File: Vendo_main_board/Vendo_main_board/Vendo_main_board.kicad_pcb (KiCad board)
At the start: 2 copper layers, 49 x 99 mm, 121 parts, among them J1 STLINK, J10 Screw_Terminal_01x04, J11 Screw_Terminal_01x04, J12 Screw_Terminal_01x02, J13 Screw_Terminal_01x02, J14 197084013, J15 197084013, J16 197084013, J17 197084013, J18 197084013, J19 FTDI, J2 Conn_01x02_Pin, J21 Conn_01x04_Pin, J23 BOOT, J5 Screw_Terminal_01x03, J6 Conn_01x06_Pin, J7 Conn_01x06_Pin, J8 Screw_Terminal_01x04, J9 Screw_Terminal_01x04, K1 SRD-05VDC-SL-C, Q3 S8050, Q4 Q_NMOS_Depletion_GSD, SW1 SW_Push, SW2 SW_DIP_x08, U1 AP64350SP-13, U10 74HC165, U11 PC817, U12 PC817, U2 AMS1117-3.3, U3 B0505S-2WR3, U4 TPL5010, U9 STM32F103C8T6, Y1 8MHz, Y2 32.768kHz

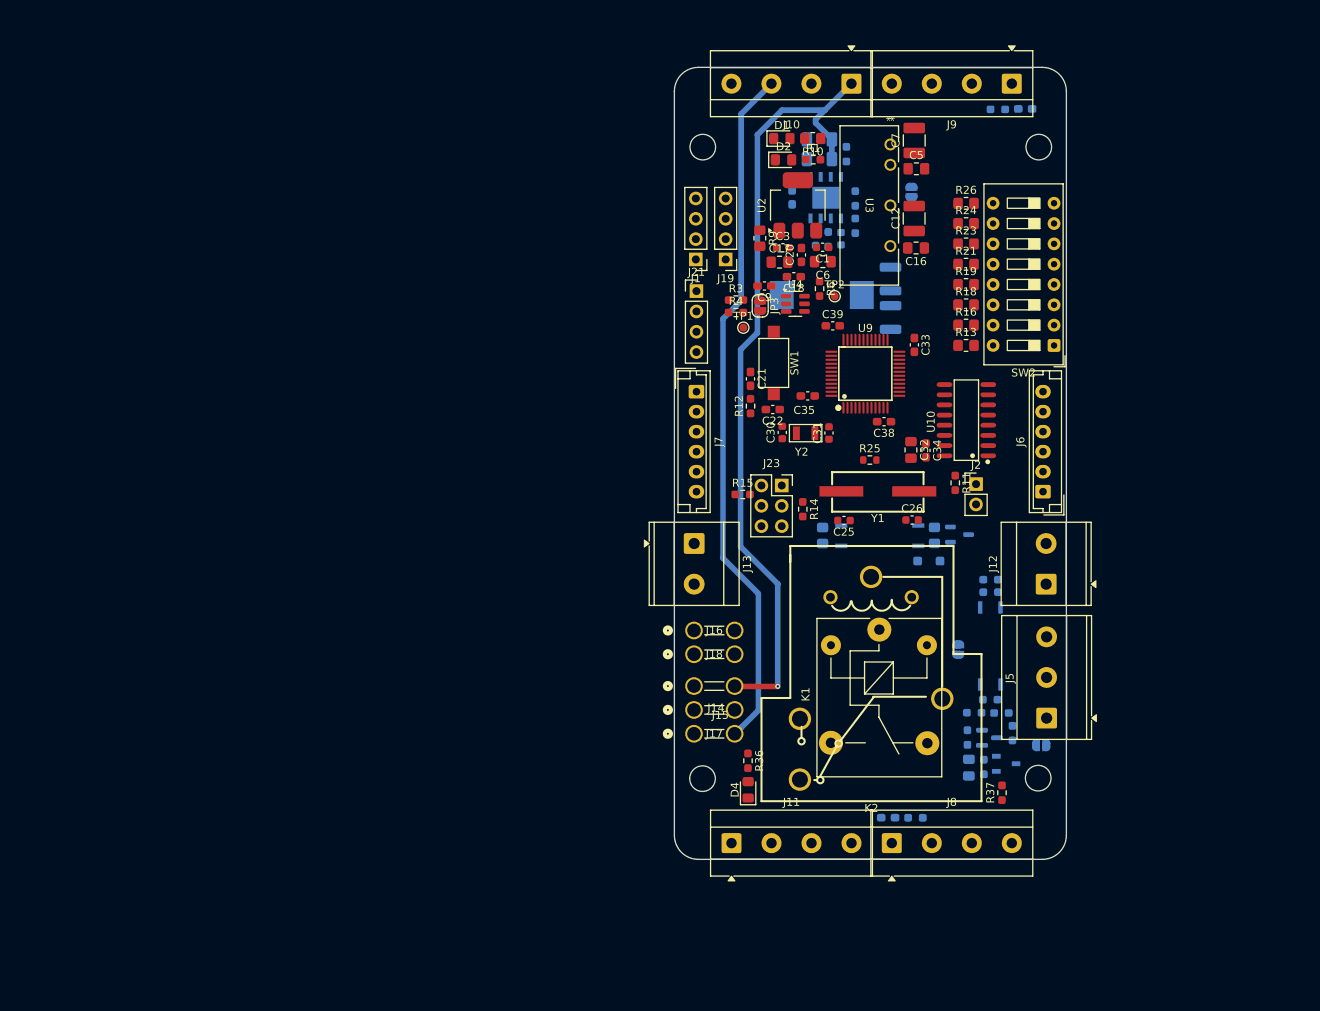
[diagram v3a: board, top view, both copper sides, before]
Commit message: -scheme update by charles
1. Used standard input and output nodes
2. Fixed GND connection of BOOT0 and BOOT1 (initially connected to Analog GND)
3. Removed redundant 100K pull up WDT RST Pin
4. Removed Nets on unconnected STM Pins
5. Fixed GND of Oscillator
6. Added 5V and 12V option to LED, removed LED as direct LED Drive
7. Renamed ESP INT to I2C INT
8. Changed 12V to 12VA, removed nets, used power rail symbol instead
9. Simplified 12V Logic
10. removed WDT, STM has internal WDT
11. Added DPDT Config to Relay Logic
12. Added Pullup I2C Line
13. Fixed 5V logic with 3.3V V Logic on 7Seg Driver
14. Added Auxiliary Pins
15.Added Debug LEDs,
Updated Footprints
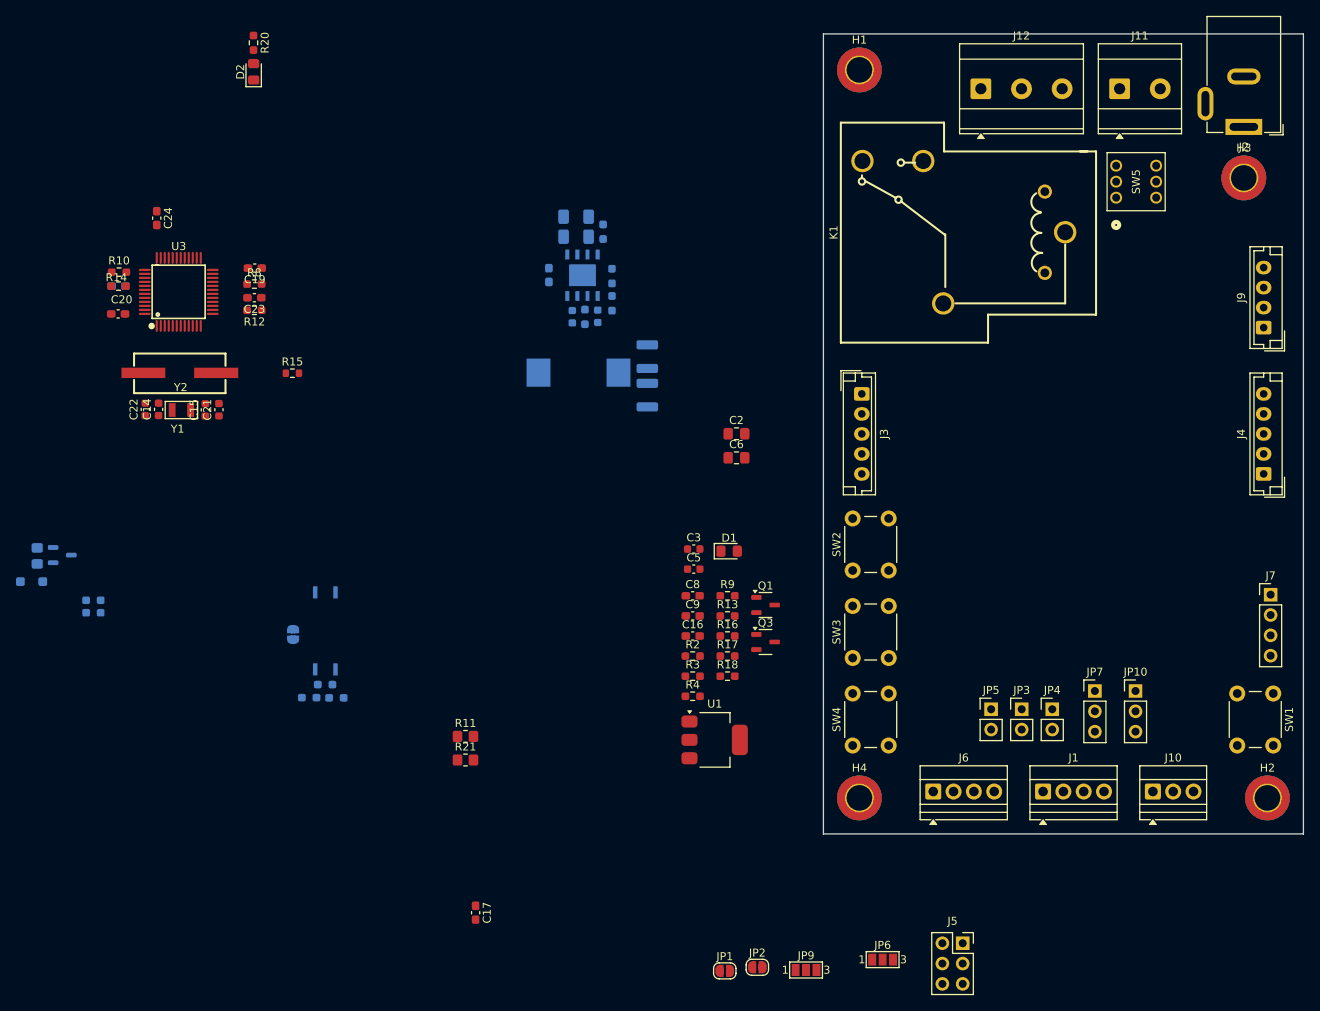
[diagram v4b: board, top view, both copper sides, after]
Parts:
- removed the C1 at (198.0, 54.3)
- removed the C12 at (209.4, 50.7)
- removed the C17 at (192.6, 56.1)
- removed the C18 at (194.4, 58.0)
- removed the C20 at (195.3, 55.2)
- removed the C22 at (191.8, 74.5)
- removed C32, C40: 10uF, Capacitor_SMD:C_0805_2012Metric_Pad1.18x1.45mm_HandSolder
- removed C34, C36: 100nF, Capacitor_SMD:C_0603_1608Metric_Pad1.08x0.95mm_HandSolder
- removed the C7 at (209.4, 40.9)
- removed the D2 at (193.1, 43.3)
- removed J13: Screw_Terminal_01x02, TerminalBlock_MetzConnect:TerminalBlock_MetzConnect_Type073_RT02602HBLU_1x02_P5.08mm_Horizontal
- removed J14, J15, J16, J17, J18: 197084013, InnovKits:Spade Conn4.8mm
- removed J19: FTDI, Connector_PinHeader_2.54mm:PinHeader_1x04_P2.54mm_Vertical
- removed J21: Conn_01x04_Pin, Connector_PinHeader_2.54mm:PinHeader_1x04_P2.54mm_Vertical
- removed the J5 at (226.0, 113.1)
- removed J8: Screw_Terminal_01x04, TerminalBlock_MetzConnect:TerminalBlock_MetzConnect_Type055_RT01504HDWU_1x04_P5.00mm_Horizontal
- removed the K1 at (205.1, 102.1)
- removed Q5: ~, footprints:SOT-23-3_L2.9-W1.6-P1.90-LS2.8-BR
- removed the R1 at (196.8, 43.3)
- removed the R10 at (196.8, 40.7)
- removed the R15 at (188.0, 85.2)
- removed the R19 at (215.9, 58.9)
- removed the R23 at (215.9, 53.9)
- removed the R24 at (215.9, 51.3)
- removed the R26 at (215.9, 48.8)
- removed R31: 10K, Resistor_SMD:R_0805_2012Metric_Pad1.20x1.40mm_HandSolder
- removed R34: 4.7k, Resistor_SMD:R_0603_1608Metric_Pad0.98x0.95mm_HandSolder
- removed R37: 1k, Resistor_SMD:R_0603_1608Metric_Pad0.98x0.95mm_HandSolder
- removed R39: 100k, Resistor_SMD:R_0603_1608Metric_Pad0.98x0.95mm_HandSolder
- removed R40: 100, Resistor_SMD:R_0603_1608Metric_Pad0.98x0.95mm_HandSolder
- removed the R6 at (197.6, 59.5)
- removed TP1, TP2: TestPoint, TestPoint:TestPoint_Pad_D1.0mm
- removed U10: 74HC165, InnovKits:SOIC-16_L9.9-W3.9-P1.27-LS6.0-BL
- removed U11: PC817, InnovKits:APC-817xx-SL_AMB
- removed the U2 at (194.9, 49.0)
- removed the U3 at (206.5, 41.4)
- removed the U4 at (194.6, 61.3)
- added C2: 1uF, Capacitor_SMD:C_0805_2012Metric_Pad1.18x1.45mm_HandSolder, F.Cu at (187.2, 77.6)
- added C8: 100nF, Capacitor_SMD:C_0603_1608Metric_Pad1.08x0.95mm_HandSolder, F.Cu at (181.8, 97.8)
- added J3: Conn_01x05_Pin, Connector_JST:JST_EH_B5B-EH-A_1x05_P2.50mm_Vertical, F.Cu at (202.9, 72.6)
- added J4: Conn_01x05_Pin, Connector_JST:JST_EH_B5B-EH-A_1x05_P2.50mm_Vertical, F.Cu at (253.1, 82.6)
- added JP10: Jumper_3_Open, Connector_PinHeader_2.54mm:PinHeader_1x03_P2.54mm_Vertical, F.Cu at (237.1, 109.7)
- added JP2: SolderJumper_2_Open, Jumper:SolderJumper-2_P1.3mm_Open_RoundedPad1.0x1.5mm, F.Cu at (189.8, 144.3)
- added JP4: SolderJumper_2_Open, Connector_PinHeader_2.54mm:PinHeader_1x02_P2.54mm_Vertical, F.Cu at (226.7, 112.0)
- added JP6: SolderJumper_3_Open, Jumper:SolderJumper-3_P1.3mm_Open_Pad1.0x1.5mm_NumberLabels, F.Cu at (205.5, 143.3)
- added JP7: Jumper_3_Open, Connector_PinHeader_2.54mm:PinHeader_1x03_P2.54mm_Vertical, F.Cu at (232.0, 109.7)
- added JP9: SolderJumper_3_Open, Jumper:SolderJumper-3_P1.3mm_Open_Pad1.0x1.5mm_NumberLabels, F.Cu at (195.9, 144.6)
- added Q1: Q_NMOS_Depletion_GSD, Package_TO_SOT_SMD:SOT-23-3, F.Cu at (190.9, 99.0)
- added R17: 100K, Resistor_SMD:R_0603_1608Metric_Pad0.98x0.95mm_HandSolder, F.Cu at (186.1, 105.4)
- added R2: 4.7K, Resistor_SMD:R_0603_1608Metric_Pad0.98x0.95mm_HandSolder, F.Cu at (181.8, 105.4)
- added SW3: SW_Push, Button_Switch_THT:SW_PUSH_6mm_H5mm, F.Cu at (201.8, 105.6)
- added SW4: SW_Push, Button_Switch_THT:SW_PUSH_6mm_H5mm, F.Cu at (201.8, 116.5)
- added SW5: SW_Slide_DPDT, InnovKits:DPDT_PUSH, F.Cu at (234.7, 48.1)
- added U1: AMS1117-3.3, Package_TO_SOT_SMD:SOT-223-3_TabPin2, F.Cu at (184.5, 115.8)
- C16: value 10uF -> 100nF; footprint Capacitor_SMD:C_0805_2012Metric_Pad1.18x1.45mm_HandSolder -> Capacitor_SMD:C_0603_1608Metric_Pad1.08x0.95mm_HandSolder
- C17: renamed from C21; value 100nF -> 1uF
- C5: value 10uF -> 22uF; footprint Capacitor_SMD:C_0805_2012Metric_Pad1.18x1.45mm_HandSolder -> Capacitor_SMD:C_0603_1608Metric
- C9: value 100nF -> 10uF
- H1, H2, H3, H4: footprint MountingHole:MountingHole_3.2mm_M3 -> MountingHole:MountingHole_3.2mm_M3_DIN965_Pad_TopBottom
- J1: value STLINK -> Screw_Terminal_01x04; footprint Connector_PinHeader_2.54mm:PinHeader_1x04_P2.54mm_Vertical -> TerminalBlock:TerminalBlock_Xinya_XY308-2.54-4P_1x04_P2.54mm_Horizontal
- J10: value Screw_Terminal_01x04 -> Screw_Terminal_01x03; footprint TerminalBlock_MetzConnect:TerminalBlock_MetzConnect_Type055_RT01504HDWU_1x04_P5.00mm_Horizontal -> TerminalBlock:TerminalBlock_Xinya_XY308-2.54-3P_1x03_P2.54mm_Horizontal
- J11: value Screw_Terminal_01x04 -> Screw_Terminal_01x02; footprint TerminalBlock_MetzConnect:TerminalBlock_MetzConnect_Type055_RT01504HDWU_1x04_P5.00mm_Horizontal -> TerminalBlock_MetzConnect:TerminalBlock_MetzConnect_Type073_RT02602HBLU_1x02_P5.08mm_Horizontal
- J12: value Screw_Terminal_01x02 -> Screw_Terminal_01x03; footprint TerminalBlock_MetzConnect:TerminalBlock_MetzConnect_Type073_RT02602HBLU_1x02_P5.08mm_Horizontal -> TerminalBlock_MetzConnect:TerminalBlock_MetzConnect_Type073_RT02603HBLU_1x03_P5.08mm_Horizontal
- J2: value Conn_01x02_Pin -> Barrel_Jack_MountingPin; footprint Connector_PinHeader_2.54mm:PinHeader_1x02_P2.54mm_Vertical -> Connector_BarrelJack:BarrelJack_GCT_DCJ200-10-A_Horizontal
- J6: value Conn_01x06_Pin -> Screw_Terminal_01x04; footprint Connector_JST:JST_EH_B6B-EH-A_1x06_P2.50mm_Vertical -> TerminalBlock:TerminalBlock_Xinya_XY308-2.54-4P_1x04_P2.54mm_Horizontal
- J7: value Conn_01x06_Pin -> FTDI; footprint Connector_JST:JST_EH_B6B-EH-A_1x06_P2.50mm_Vertical -> Connector_PinHeader_2.54mm:PinHeader_1x04_P2.54mm_Vertical
- J9: value Screw_Terminal_01x04 -> Conn_01x04_Pin; footprint TerminalBlock_MetzConnect:TerminalBlock_MetzConnect_Type055_RT01504HDWU_1x04_P5.00mm_Horizontal -> Connector_JST:JST_EH_B4B-EH-A_1x04_P2.50mm_Vertical
- JP1: moved to F.Cu
- JP3: footprint Jumper:SolderJumper-2_P1.3mm_Open_RoundedPad1.0x1.5mm -> Connector_PinHeader_2.54mm:PinHeader_1x02_P2.54mm_Vertical
- JP5: footprint Jumper:SolderJumper-2_P1.3mm_Open_RoundedPad1.0x1.5mm -> Connector_PinHeader_2.54mm:PinHeader_1x02_P2.54mm_Vertical; moved to F.Cu
- Q3: value S8050 -> Q_NMOS_Depletion_GSD; footprint Package_TO_SOT_SMD:SOT-23 -> Package_TO_SOT_SMD:SOT-23-3; moved to F.Cu
- R10: renamed from R29; value 1k -> 1K; moved to F.Cu
- R11: value 1k -> 10K; footprint Resistor_SMD:R_0603_1608Metric_Pad0.98x0.95mm_HandSolder -> Resistor_SMD:R_0805_2012Metric_Pad1.20x1.40mm_HandSolder
- R12: value 1k -> 10K
- R13, R16, R18: footprint Resistor_SMD:R_0805_2012Metric_Pad1.20x1.40mm_HandSolder -> Resistor_SMD:R_0603_1608Metric_Pad0.98x0.95mm_HandSolder
- R14: renamed from R30; moved to F.Cu
- R20: renamed from R36; value 1k -> 1K
- R22: renamed from R32; value 1k -> 1K
- R24: renamed from R35; value 1k -> 1K
- R25: renamed from R41; value 1k -> 1K
- R3: value 10K -> 4.7K
- R4: value 40.2K -> 1K
- R9: value 3.3K -> 100k; footprint Resistor_SMD:R_0805_2012Metric_Pad1.20x1.40mm_HandSolder -> Resistor_SMD:R_0603_1608Metric_Pad0.98x0.95mm_HandSolder
- SW1: footprint Button_Switch_SMD:SW_SPST_CK_RS282G05A3 -> Button_Switch_THT:SW_PUSH_6mm_H5mm
- SW2: value SW_DIP_x08 -> SW_Push; footprint Button_Switch_THT:SW_DIP_SPSTx08_Slide_9.78x22.5mm_W7.62mm_P2.54mm -> Button_Switch_THT:SW_PUSH_6mm_H5mm
- moved R10 120.7 mm to (110.1, 57.4), turned to 0 degrees
- moved C18 115.5 mm to (110.0, 59.1), turned to 0 degrees
- moved Q2 112.2 mm to (103.0, 92.8)
- moved D3 112.2 mm to (99.1, 96.1)
- moved R25 112.2 mm to (106.8, 100.0)
- moved R26 112.2 mm to (106.8, 98.4)
- moved R19 112.2 mm to (99.8, 92.9)
- moved R14 112.1 mm to (110.0, 59.1)
- moved D2 109.0 mm to (126.9, 32.3)
- moved R20 109.0 mm to (126.9, 28.7)
- moved J11 106.0 mm to (235.1, 34.5)
- moved H3 101.1 mm to (250.7, 45.6)
- moved JP1 100.1 mm to (185.8, 144.7), turned to 0 degrees
- moved J10 96.2 mm to (239.3, 122.3), turned to 0 degrees
- moved Y2 88.5 mm to (117.6, 70.0)
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- renumbered C2 to C1, C13 to C12, C19 to C13, C30 to C14, C31 to C15, C37 to C18, C33 to C19, C35 to C20, C26 to C21, C25 to C22, C38 to C23, C39 to C24, C8 to C7, D4 to D2, D5 to D3, J23 to J5, JP4 to JP8, K2 to K1, Q4 to Q2, R2 to R1, R25 to R15, R38 to R19, R33 to R23, R42 to R26, R8 to R6, R14 to R8, U1 to U2, U9 to U3, U12 to U4, Y2 to Y1, Y1 to Y2
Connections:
- net /PC14 renamed Net-(U3-PC14-OSC32_IN)
- net /PC15 renamed Net-(U3-PC15-OSC32_OUT)
- net /STM32_IN1 renamed COIN_IN
- C1 pad 1: 12V -> 12V_OUT
- C1 pad 2: GNDPWR -> GND
- C10 pad 2: GNDPWR -> GND
- C11 pad 2: GNDPWR -> GND
- C12 pad 1: +5VA -> +5V
- C13 pad 1: +5VA -> +5V
- C13 pad 2: GNDPWR -> GND
- C16 pad 1: GNDD -> +3.3V
- C16 pad 2: +5V -> GND
- C17 pad 1: GNDD -> GND
- C17 pad 2: /STM_RST -> STM_RST
- C18 pad 1: GNDD -> GND
- C18 pad 2: /ESP_INT -> I2C_INT
- C19 pad 1: GNDD -> GND
- C20 pad 1: GNDD -> GND
- C21 pad 2: /OSCOUT -> Net-(U3-PD0_OSC_IN)
- C22 pad 2: /OSCIN -> Net-(U3-PD1_OSC_OUT)
- C23 pad 1: GNDD -> GND
- C24 pad 1: GNDD -> GND
- C3 pad 1: GNDD -> GND
- C3 pad 2: +3.3V -> +5V
- C4 pad 1: 12V -> 12V_OUT
- C4 pad 2: GNDPWR -> GND
- C5 pad 1: GNDPWR -> GND
- C5 pad 2: +5VA -> +3.3V
- C6 pad 1: GNDD -> GND
- C6 pad 2: +5V -> +3.3V
- C9 pad 1: +3.3V -> GND
- C9 pad 2: GNDD -> +3.3V
- D1 pad 1: GNDPWR -> Net-(D1-K)
- D1 pad 2: Net-(D1-A) -> +3.3V
- J1 pad 1: +3.3V -> USER_BTN
- J1 pad 2: /STM32_SWDIO -> GND
- J1 pad 3: /STM32_SWCLK -> Net-(J1-Pin_3)
- J1 pad 4: GNDD -> Net-(J1-Pin_4)
- J10 pad 1: 12V -> Net-(J10-Pin_1)
- J10 pad 2: GNDPWR -> Net-(J10-Pin_2)
- J10 pad 3: /EXT -> 12V_OUT
- J11 pad 1: /12V_SEL -> GND_OUT
- J11 pad 2: /COM -> 12V_OUT
- J12 pad 1: GNDPWR -> RLY_NC
- J12 pad 2: /12V_SEL -> RLY_COM
- J2 pad 1: /I2C_CONF -> 12V_OUT
- J2 pad 2: GNDD -> GND
- J5 pad 4: Net-(J23-Pin_4) -> Net-(J5-Pin_4)
- J6 pad 1: GNDD -> Net-(J6-Pin_1)
- J6 pad 2: /STM32_SCL -> AUX_1
- J6 pad 3: /STM32_SDA -> AUX_2
- J6 pad 4: /ESP_INT -> GND
- J7 pad 1: +5VA -> +5V
- J7 pad 2: GNDPWR -> STM_TX
- J7 pad 3: /ESP_INT -> STM_RX
- J7 pad 4: /STM32_SDA -> GND
- J9 pad 1: /ESP_INT -> Net-(J9-Pin_1)
- J9 pad 2: /STM32_SCL -> SEG_CLK
- J9 pad 3: /STM32_SDA -> SEG_DIO
- J9 pad 4: GNDD -> GND
- JP1 pad 1: +5VA -> STM_SCL
- JP1 pad 2: +5V -> Net-(JP1-B)
- JP3 pad 1: Net-(JP3-A) -> Net-(J1-Pin_3)
- JP3 pad 2: Net-(JP3-B) -> 12V_OUT
- JP5 pad 1: 12V -> Net-(J1-Pin_3)
- JP5 pad 2: /12VA -> +3.3V
- JP8 pad 1: Net-(J5-Pin_2) -> Net-(J10-Pin_2)
- K1 pad 1: /12V_SEL -> RLY_NC
- K1 pad 2: /12V_SEL -> RLY_NO
- K1 pad 5: /COM -> RLY_COM
- K1 pad 6: /COM -> RLY_COM
- L1 pad 2: +5VA -> +5V
- Q2 pad 1: Net-(Q4-G) -> RLY_DRV
- Q2 pad 2: GNDPWR -> GND
- Q3 pad 1: Net-(Q3-B) -> COIN_EN
- Q3 pad 2: GNDPWR -> GND
- R1 pad 2: GNDPWR -> GND
- R10 pad 2: /BUTTON_1 -> USER_BTN
- R11 pad 1: +3.3V -> USER_LED
- R11 pad 2: /I2C_CONF -> GND
- R12 pad 2: /STM_RST -> STM_RST
- R13 pad 1: +5V -> +3.3V
- R13 pad 2: Net-(U10-D0) -> BTN_MODE_1
- R14 pad 2: /ESP_INT -> I2C_INT
- R15 pad 1: /OSCIN -> Net-(U3-PD1_OSC_OUT)
- R15 pad 2: /OSCOUT -> Net-(U3-PD0_OSC_IN)
- R16 pad 1: +5V -> +3.3V
- R16 pad 2: Net-(U10-D1) -> BTN_MODE_2
- R18 pad 1: +5V -> +3.3V
- R18 pad 2: Net-(U10-D2) -> BTN_MODE_3
- R19 pad 1: Net-(Q4-G) -> RLY_DRV
- R19 pad 2: GNDPWR -> GND
- R21 pad 1: +5V -> COIN_EN
- R21 pad 2: Net-(U10-D4) -> GND
- R22 pad 2: Net-(J5-Pin_2) -> Net-(J10-Pin_2)
- R23 pad 1: GNDPWR -> GND
- R23 pad 2: Net-(J5-Pin_2) -> Net-(J10-Pin_2)
- R24 pad 1: Net-(J5-Pin_2) -> Net-(J10-Pin_2)
- R26 pad 1: GNDD -> GND
- R3 pad 1: GNDD -> +3.3V
- R3 pad 2: Net-(JP3-A) -> Net-(JP2-B)
- R4 pad 1: GNDD -> Net-(D1-K)
- R4 pad 2: Net-(JP3-B) -> GND
- R6 pad 2: GNDPWR -> GND
- R7 pad 1: +5VA -> +5V
- R8 pad 1: /STM32_BOOT1 -> STM_BOOT0
- R9 pad 1: +3.3V -> STM_BOOT1
- R9 pad 2: GNDD -> Net-(J5-Pin_4)
- SW1 pad 1: GNDD -> STM_RST
- SW1 pad 2: /STM_RST -> GND
- SW2 pad 1: GNDD -> GND
- SW2 pad 2: GNDD -> BTN_MODE_1
- U2 pad 2: 12V -> 12V_OUT
- U2 pad 3: 12V -> 12V_OUT
- U2 pad 7: GNDPWR -> GND
- U2 pad EPAD: GNDPWR -> GND
- U3 pad 1: /VBAT -> +3.3V
- U3 pad 12: /UART_TX1 -> unconnected-(U3-PA2-Pad12)
- U3 pad 13: /UART_RX1 -> unconnected-(U3-PA3-Pad13)
- U3 pad 14: /EN_COIN -> COIN_EN
- U3 pad 16: /DC_DRV_1 -> RLY_DRV
- U3 pad 17: /WDT_DONE -> WDT_DONE
- U3 pad 18: unconnected-(U9-PB0-Pad18) -> AUX_1
- U3 pad 19: unconnected-(U9-PB1-Pad19) -> AUX_2
- U3 pad 20: /STM32_BOOT1 -> STM_BOOT1
- U3 pad 21: /SEG_CLK -> SEG_CLK
- U3 pad 22: /SEG_DIO -> SEG_DIO
- U3 pad 23: GNDD -> GND
- U3 pad 26: /TMR_CLK -> BTN_MODE_1
- U3 pad 27: /TMR_LOAD -> BTN_MODE_2
- U3 pad 28: /TMR_DATA -> BTN_MODE_3
- U3 pad 29: /I2C_CONF -> I2C_CONFG
- U3 pad 30: /STM32_TX -> STM_TX
- U3 pad 31: /STM32_RX -> STM_RX
- U3 pad 32: /PA11 -> unconnected-(U3-PA11-Pad32)
- U3 pad 33: /PA12 -> unconnected-(U3-PA12-Pad33)
- U3 pad 34: /STM32_SWDIO -> unconnected-(U3-PA13-Pad34)
- U3 pad 35: GNDD -> GND
- U3 pad 37: /STM32_SWCLK -> unconnected-(U3-PA14-Pad37)
- U3 pad 39: /BUTTON_1 -> USER_BTN
- U3 pad 40: /LED_P -> USER_LED
- U3 pad 41: /ESP_INT -> I2C_INT
- U3 pad 42: /STM32_SCL -> STM_SCL
- U3 pad 43: /STM32_SDA -> STM_SDA
- U3 pad 44: /STM32_BOOT0 -> STM_BOOT0
- U3 pad 46: /CTRL_DCI1 -> unconnected-(U3-PB9-Pad46)
- U3 pad 47: GNDD -> GND
- U3 pad 5: /OSCIN -> Net-(U3-PD0_OSC_IN)
- U3 pad 6: /OSCOUT -> Net-(U3-PD1_OSC_OUT)
- U3 pad 7: /STM_RST -> STM_RST
- U3 pad 8: GNDD -> GND
- U4 pad 2: GNDPWR -> GND
- U4 pad 3: GNDD -> GND
- Y2 pad 1: /OSCOUT -> Net-(U3-PD0_OSC_IN)
- Y2 pad 2: /OSCIN -> Net-(U3-PD1_OSC_OUT)
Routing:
- net 12V: track 99.0 -> 0.00 mm, vias 1 -> 0
- net /EXT: track 86.9 -> 0.00 mm
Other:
- board size 49 x 99 mm -> 60 x 100 mm

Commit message: -scheme minor edit -parts placement
-remove 5VA to 5V , relay part and coin part
-place components on the pcb for proposal
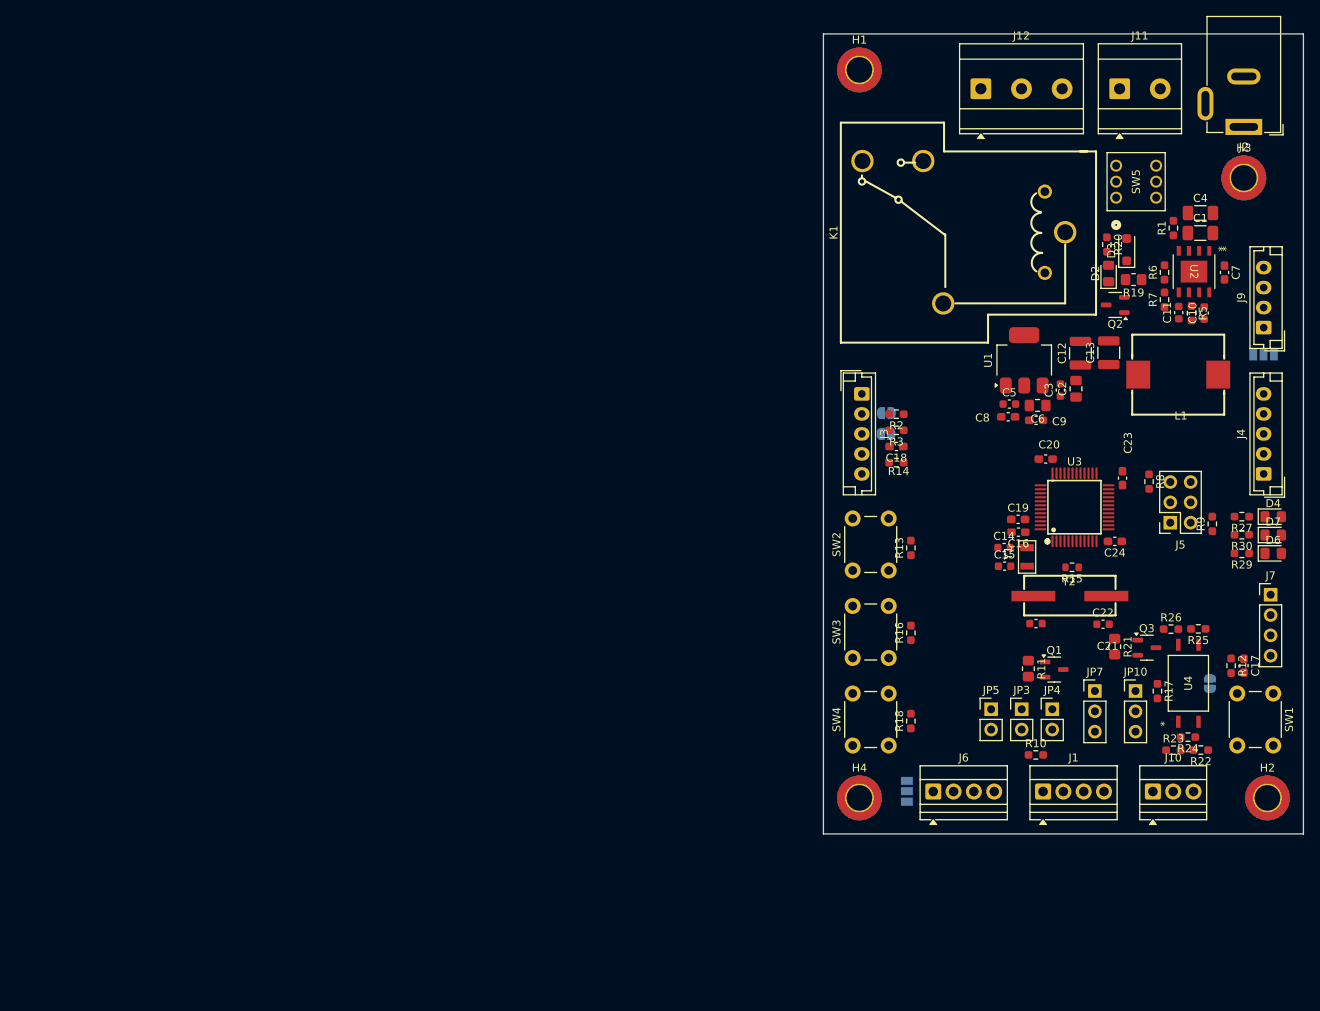
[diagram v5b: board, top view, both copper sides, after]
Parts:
- removed D1: LED, LED_SMD:LED_0805_2012Metric_Pad1.15x1.40mm_HandSolder
- removed R4: 1K, Resistor_SMD:R_0603_1608Metric_Pad0.98x0.95mm_HandSolder
- added D4: LED, LED_SMD:LED_0805_2012Metric_Pad1.15x1.40mm_HandSolder, F.Cu at (254.3, 87.9)
- added D6: LED, LED_SMD:LED_0805_2012Metric_Pad1.15x1.40mm_HandSolder, F.Cu at (254.3, 92.5)
- added D7: LED, LED_SMD:LED_0805_2012Metric_Pad1.15x1.40mm_HandSolder, F.Cu at (254.3, 90.2)
- added R27: 1K, Resistor_SMD:R_0603_1608Metric_Pad0.98x0.95mm_HandSolder, F.Cu at (250.4, 87.9)
- added R29: 1K, Resistor_SMD:R_0603_1608Metric_Pad0.98x0.95mm_HandSolder, F.Cu at (250.4, 92.5)
- added R30: 1K, Resistor_SMD:R_0603_1608Metric_Pad0.98x0.95mm_HandSolder, F.Cu at (250.4, 90.2)
- C1, C10, C11, C12, C13, C18, C4, C7, D3, L1, Q2, R1, R19, R22, R23, R24, R25, R26, R5, R6, R7, U2, U4: moved to F.Cu
- JP1, JP2, JP6, JP9: moved to B.Cu
- moved D3 143.0 mm to (236.0, 54.6), turned to 90 degrees
- moved R19 141.3 mm to (236.9, 58.3), turned to 180 degrees
- moved R25 138.1 mm to (245.0, 102.0), turned to 180 degrees
- moved Q2 135.3 mm to (234.6, 61.5), turned to 180 degrees
- moved R26 134.8 mm to (241.6, 102.0)
- moved R12 129.9 mm to (249.1, 106.6), turned to -90 degrees
- moved R10 129.5 mm to (224.6, 117.7)
- moved C24 126.4 mm to (234.5, 91.0), turned to 180 degrees
- moved C22 122.7 mm to (233.1, 101.4), turned to 0 degrees
- moved C20 117.4 mm to (225.9, 80.7)
- moved U3 115.2 mm to (229.5, 86.8)
- moved JP8 114.8 mm to (246.4, 108.8)
- moved Y2 114.7 mm to (228.9, 97.9), turned to 0 degrees
- moved R8 114.5 mm to (238.8, 83.6), turned to -90 degrees
- moved R22 111.7 mm to (245.3, 117.1), turned to 180 degrees
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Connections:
- net 12V_OUT renamed +12V
- D3 pad 2: +5VA -> +5V
- K1 pad 3: +5VA -> +5V
- R20 pad 1: +5VA -> +5V
- R22 pad 1: +5VA -> +5V
- U3 pad 12: unconnected-(U3-PA2-Pad12) -> DBG_LED_G
- U3 pad 13: unconnected-(U3-PA3-Pad13) -> DBG_LED_B
- U3 pad 17: WDT_DONE -> unconnected-(U3-PA7-Pad17)
